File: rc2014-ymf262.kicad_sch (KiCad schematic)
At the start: 17 parts, among them CON1 SJ1-3523N, P1 RC2014 BUS, U1 74HCT688, U2 YM3812, U3 YM3014B, U4 LM358, X1 3.579545MHz

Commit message: initial work on schematic
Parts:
- removed U2: YM3812, Package_DIP:DIP-24_W15.24mm, symbol electrified:YM3812
- removed U3: YM3014B, Package_DIP:DIP-8_W7.62mm, symbol electrified:YM3014B
- added R1: R, symbol Device:R
- added U2: YMF262, Package_SO:SOP-24_7.5x15.4mm_P1.27mm, symbol electrified:YMF262
- added U3: LM358, Package_DIP:DIP-8_W7.62mm, symbol Amplifier_Operational:LM358
- added U5: YAC512, Package_SO:SOP-16_4.55x10.3mm_P1.27mm, symbol electrified:YAC512
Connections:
- net A0: now also U2.4 (A_{0})
- net A1: now also U2.5 (A_{1}); no longer U1.15 (P6)
- net CLK: now also U2.24 (ΦM)
- net D0: now also U2.10 (D_{0})
- net D1: now also U2.11 (D_{1})
- net D2: now also U2.13 (D_{2})
- net D3: now also U2.14 (D_{3})
- net D4: now also U2.15 (D_{4})
- net D5: now also U2.16 (D_{5})
- net D6: now also U2.17 (D_{6})
- net D7: now also U2.18 (D_{7})
- net DAC_CLK: now also U2.23 (ΦSY), U5.5 (CLK)
- net GND: now also U1.15 (P6), U1.16 (R6), U2.12 (GND), U3.4 (V-), U5.2 (GND), U5.6 (FSEL), U5.9 (TST1)
- net VCC: now also U2.1 (VDD), U3.8 (V+), U5.1 (VDD), U5.3 (VDD)
- net ~{CS}: now also U2.8 (~{CS})
- net ~{INT}: now also U2.2 (~{IRQ})
- net ~{RD}: now also U2.7 (~{RD})
- net ~{RESET}: now also U2.3 (~{IC})
- net ~{WR}: now also U2.6 (~{WR})
- net at JP1.14 (Pin_14), RN1.8 (R7): no longer U1.16 (R6)
- net at C6.1, U4.5 (+): now also U5.16 (CV)
- net at U4.6 (-), U4.7: now also U5.14 (MP); no longer C5.1
- net TO_BUFF: no longer names the net of U4.3 (+)
- net TO_BUFF: now also C5.1, U5.13 (AOUT)
- new net: U3.3 (+), U5.11 (CH2)
- new net: U3.5 (+), U5.10 (CH1)
- new net: R1.1, U5.12 (SWIN)
- new net: R1.2, U4.1, U4.2 (-)
- new net DOAB: U2.21 (DOAB), U5.4 (DIN)
- new net L: CON1.T, CON1.TN, U3.1, U3.2 (-)
- new net R: CON1.R, CON1.RN, U3.6 (-), U3.7
- new net SMPAC: U2.20 (SMPAC), U5.8 (SMP1)
- new net SMPBD: U2.19 (SMPBD), U5.7 (SMP2)
- no-connect marks 17 -> 19
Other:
- moved on the sheet: U4B, X1

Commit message: move to use mostly SMD
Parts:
- removed C1: 4.7uF, Capacitor_THT:CP_Radial_D7.5mm_P2.50mm, symbol Device:C_Polarized_Small
- removed U3, U4: LM358, Package_DIP:DIP-8_W7.62mm, symbol Amplifier_Operational:LM358
- added U6: TL074, Package_SO:SOIC-14_3.9x8.7mm_P1.27mm, symbol Amplifier_Operational:TL074
- C2, C3, C4, C7: footprint Capacitor_THT:C_Disc_D3.8mm_W2.6mm_P2.50mm -> Capacitor_SMD:C_0603_1608Metric_Pad1.08x0.95mm_HandSolder
- JP1: footprint Connector_PinHeader_2.54mm:PinHeader_2x08_P2.54mm_Horizontal -> Connector_PinHeader_2.54mm:PinHeader_2x06_P2.54mm_Horizontal; symbol Connector_Generic:Conn_02x08_Odd_Even -> Connector_Generic:Conn_02x06_Odd_Even
- R1: footprint (none) -> Resistor_SMD:R_0603_1608Metric_Pad0.98x0.95mm_HandSolder
- RN1: footprint Resistor_THT:R_Array_SIP9 -> Resistor_SMD:R_Array_Convex_8x0602; symbol Device:R_Network08 -> Device:R_Network06
- U1: footprint Package_DIP:DIP-20_W7.62mm_Socket -> Package_SO:SOIC-20W_7.5x12.8mm_P1.27mm
- X1: value 3.579545MHz -> 14.318MHz
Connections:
- net GND: now also U6.11 (V-)
- net L: now also U6.8, U6.9 (-)
- net R: now also U6.13 (-), U6.14
- net VCC: now also U6.4 (V+); no longer JP1.13 (Pin_13), JP1.15 (Pin_15)
- net at C6.1, U5.16 (CV): now also U6.3 (+)
- net at U5.11 (CH2): now also U6.10 (+)
- net at U5.10 (CH1): now also U6.12 (+)
- net at C5.1, U5.13 (AOUT): now also U6.5 (+)
- net at U5.14 (MP): now also U6.1, U6.2 (-)
- net at R1.2: now also U6.6 (-), U6.7

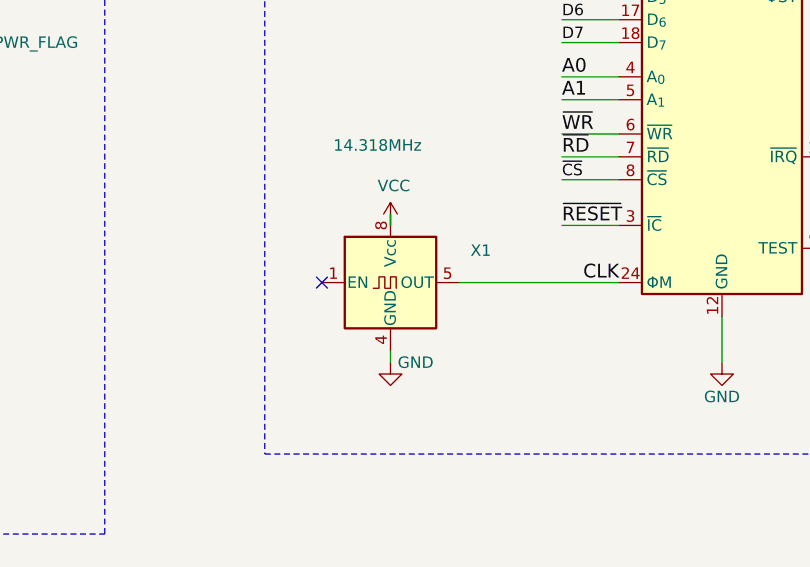
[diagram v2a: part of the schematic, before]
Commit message: use custom oscillator footprint
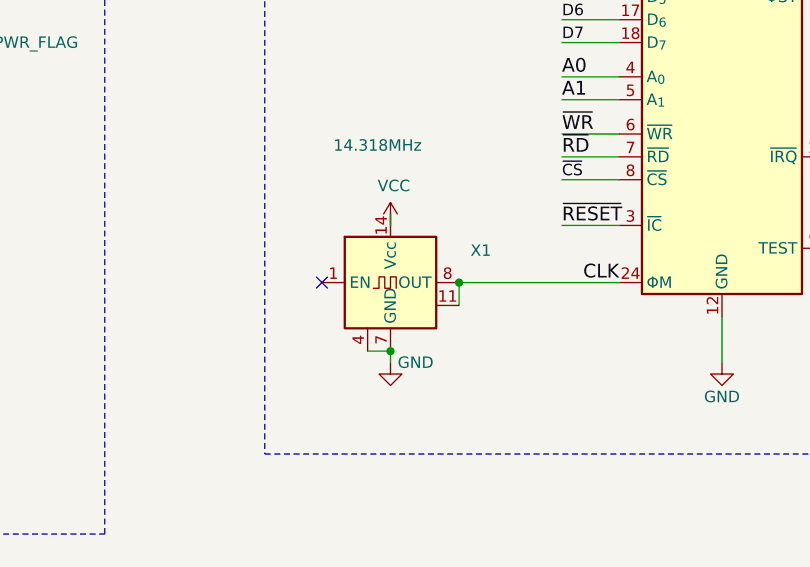
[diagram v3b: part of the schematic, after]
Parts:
- X1: footprint Package_DIP:DIP-8_W7.62mm_Socket -> electrified:Oscillator_DIP-8-14; symbol Oscillator:CXO_DIP8 -> electrified:CXO_DIP-8-14
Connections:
- net CLK: now also X1.11, X1.8 (OUT); no longer X1.5 (OUT)
- net GND: now also X1.7 (GND)
- net VCC: now also X1.14 (Vcc); no longer X1.8 (Vcc)
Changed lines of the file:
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@@
 	)
 	(junction
+		(at 124.46 198.12)
+		(diameter 0)
+		(color 0 0 0 0)
+	)
+	(junction
+		(at 116.84 205.74)
+		(diameter 0)
+		(color 0 0 0 0)
+	)
+	(junction
 		(at 278.13 123.19)
 		(diameter 0)
@@
 		)
 	)
+	(wire
+		(pts
+			(xy 114.3 205.74) (xy 116.84 205.74)
+		)
+		(stroke
+			(width 0)
+			(type default)
+		)
+	)
 	(polyline
 		(pts
@@
 	(wire
 		(pts
+			(xy 124.46 198.12) (xy 124.46 200.66)
+		)
+		(stroke
+			(width 0)
+			(type default)
+		)
+	)
+	(wire
+		(pts
 			(xy 337.82 143.51) (xy 342.9 143.51)
 		)
@@
 	)
 	(symbol
-		(lib_id "Oscillator:CXO_DIP8")
+		(lib_id "electrified:CXO_DIP-8-14")
 		(at 116.84 198.12 0)
 		(unit 1)
@@
 			)
 		)
-		(property "Footprint" "Package_DIP:DIP-8_W7.62mm_Socket"
-			(at 128.27 207.01 0)
+		(property "Footprint" "electrified:Oscillator_DIP-8-14"
+			(at 116.84 179.07 0)
 			(effects
 				(font
@@
 		)
 		(property "Datasheet" "http://cdn-reichelt.de/documents/datenblatt/B400/OSZI.pdf"
-			(at 114.3 198.12 0)
+			(at 116.84 198.12 0)
 			(effects
 				(font
@@
 		(pin "4"
 		)
-		(pin "5"
+		(pin "11"
 		)
 		(pin "8"
 		)
+		(pin "7"
+		)
+		(pin "14"
+		)
 		(instances

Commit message: more work on schematic and layout
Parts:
- added C1: 10nF, Capacitor_SMD:C_0603_1608Metric_Pad1.08x0.95mm_HandSolder, symbol Device:C_Small
- added C10, C11: 2.7nf, Capacitor_SMD:C_0603_1608Metric_Pad1.08x0.95mm_HandSolder, symbol Device:C_Small
- added C12, C14: 10uf, Capacitor_SMD:C_0603_1608Metric_Pad1.08x0.95mm_HandSolder, symbol Device:C_Polarized_Small
- added C13, C9: 10uF, Capacitor_SMD:C_1206_3216Metric, symbol Device:C_Polarized_Small
- added C15: 100nf, Capacitor_SMD:C_0603_1608Metric_Pad1.08x0.95mm_HandSolder, symbol Device:C_Small
- added C16, C17: 470pF, Capacitor_SMD:C_0603_1608Metric_Pad1.08x0.95mm_HandSolder, symbol Device:C_Small
- added C18, C19: 3.9nF, Capacitor_SMD:C_0603_1608Metric_Pad1.08x0.95mm_HandSolder, symbol Device:C_Small
- added C8: 100nF, Capacitor_SMD:C_0603_1608Metric_Pad1.08x0.95mm_HandSolder, symbol Device:C_Small
- added L1: BLM18PG221SN1D, Inductor_SMD:L_0603_1608Metric_Pad1.05x0.95mm_HandSolder, symbol Device:L
- added L2: 33uH, Inductor_SMD:L_0603_1608Metric_Pad1.05x0.95mm_HandSolder, symbol Device:L
- added R2, R3: 15k, Resistor_SMD:R_0603_1608Metric_Pad0.98x0.95mm_HandSolder, symbol Device:R
- added R4, R5: 1K, Resistor_SMD:R_0603_1608Metric_Pad0.98x0.95mm_HandSolder, symbol Device:R
- C5: value 10uF -> 68pf; footprint Capacitor_THT:C_Radial_D4.0mm_H7.0mm_P1.50mm -> Capacitor_SMD:C_0603_1608Metric_Pad1.08x0.95mm_HandSolder
- C6: footprint Capacitor_THT:C_Radial_D4.0mm_H7.0mm_P1.50mm -> Capacitor_SMD:C_0603_1608Metric_Pad1.08x0.95mm_HandSolder
- H1: now left out of the parts list
- JP1: footprint Connector_PinHeader_2.54mm:PinHeader_2x06_P2.54mm_Horizontal -> Connector_PinHeader_2.54mm:PinHeader_2x06_P2.54mm_Vertical
- R1: value R -> 33
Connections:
- net GND: now also C1.2, C10.2, C11.2, C13.2, C15.2, C18.2, C19.2, C8.2, C9.2; no longer U5.6 (FSEL), U5.9 (TST1)
- net L: now also C12.1, C16.1, R2.2; no longer CON1.T, CON1.TN, U6.9 (-)
- net R: now also C14.1, C17.2, R3.2; no longer CON1.R, CON1.RN, U6.13 (-)
- net VCC: now also JP1.10 (Pin_10), JP1.12 (Pin_12), JP1.2 (Pin_2), JP1.4 (Pin_4), JP1.6 (Pin_6), JP1.8 (Pin_8); no longer C4.1, C7.1, JP1.1 (Pin_1), JP1.11 (Pin_11), JP1.3 (Pin_3), JP1.5 (Pin_5), JP1.7 (Pin_7), JP1.9 (Pin_9), U5.1 (VDD), U5.3 (VDD), U6.4 (V+)
- net ~{INT}: no longer U2.2 (~{IRQ})
- net at RN1.6 (R5), U1.12 (R4): now also JP1.3 (Pin_3); no longer JP1.10 (Pin_10)
- net at RN1.7 (R6), U1.14 (R5): now also JP1.1 (Pin_1); no longer JP1.12 (Pin_12)
- net at RN1.2 (R1), U1.3 (R0): now also JP1.11 (Pin_11); no longer JP1.2 (Pin_2)
- net at RN1.3 (R2), U1.5 (R1): now also JP1.9 (Pin_9); no longer JP1.4 (Pin_4)
- net at RN1.4 (R3), U1.7 (R2): now also JP1.7 (Pin_7); no longer JP1.6 (Pin_6)
- net at RN1.5 (R4), U1.9 (R3): now also JP1.5 (Pin_5); no longer JP1.8 (Pin_8)
- net at U5.10 (CH1), U6.12 (+): now also C11.1
- net at U5.11 (CH2), U6.10 (+): now also C10.1
- new net: C8.1, C9.1, L1.1, L2.2
- new net: C19.1, CON1.R, CON1.RN, R5.2
- new net: C18.1, CON1.T, CON1.TN, R4.2
- new net: C12.2, R4.1
- new net: C17.1, R3.1, U6.13 (-)
- new net: C16.2, R2.1, U6.9 (-)
- new net: C14.2, R5.1
- new net +5V: C1.1, L1.2
- new net +5VA: C13.1, C15.1, C4.1, C7.1, L2.1, U5.1 (VDD), U5.3 (VDD), U5.6 (FSEL), U5.9 (TST1), U6.4 (V+)
- no-connect marks 19 -> 20
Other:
- moved on the sheet: C2, C3, C4, C5, C6, C7, CON1, JP1, P1, R1, RN1, U1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

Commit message: add additional docs and other random updates
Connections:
- no-connect marks 20 -> 21
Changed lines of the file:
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@@
+	)
+	(no_connect
+		(at 147.32 153.67)
 	)
 	(no_connect
@@
 	(polyline
 		(pts
-			(xy 384.81 46.99) (xy 196.85 46.99)
+			(xy 384.81 46.99) (xy 195.58 46.99)
 		)
 		(stroke
@@
 	(polyline
 		(pts
-			(xy 195.58 45.72) (xy 195.58 210.82)
+			(xy 195.58 46.99) (xy 195.58 212.09)
 		)
 		(stroke
@@
 	(polyline
 		(pts
-			(xy 196.85 45.72) (xy 195.58 45.72)
-		)
-		(stroke
-			(width 0)
-			(type dash)
-		)
-	)
-	(polyline
-		(pts
 			(xy 252.73 256.54) (xy 252.73 279.4)
 		)
@@
 		)
 		(stroke
-			(width 0)
-			(type default)
-		)
-	)
-	(wire
-		(pts
-			(xy 147.32 153.67) (xy 157.48 153.67)
-		)
-		(stroke
